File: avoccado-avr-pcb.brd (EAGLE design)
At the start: 17.8 x 33 mm, 32 parts, among them IC1 MCP1703CB, Q1 #MHz, Q2 MOSFET-NCHANNEL2N7002PW, U1 ATMEGA168#, U2 MCP73831, X1 Micro USB

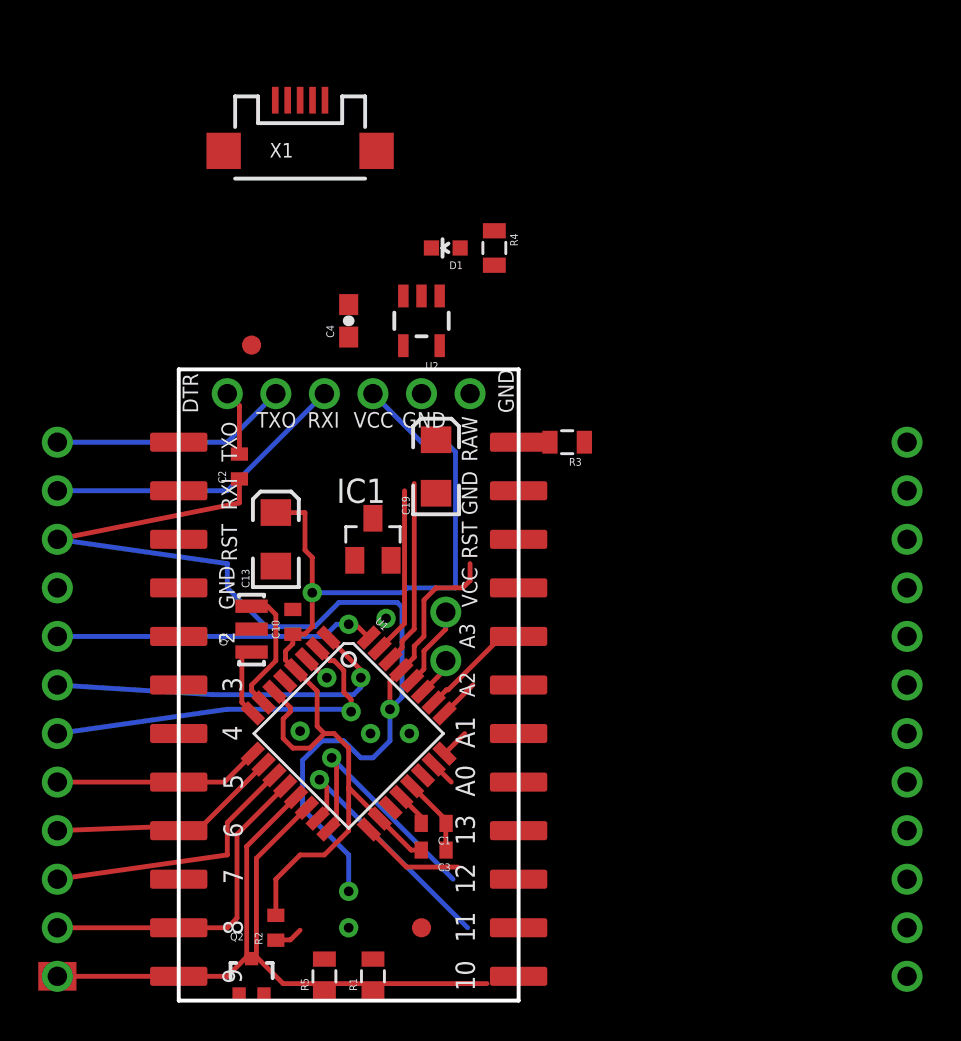
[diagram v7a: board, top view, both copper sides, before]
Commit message: squeezed the headers together to make the PCB even thinner
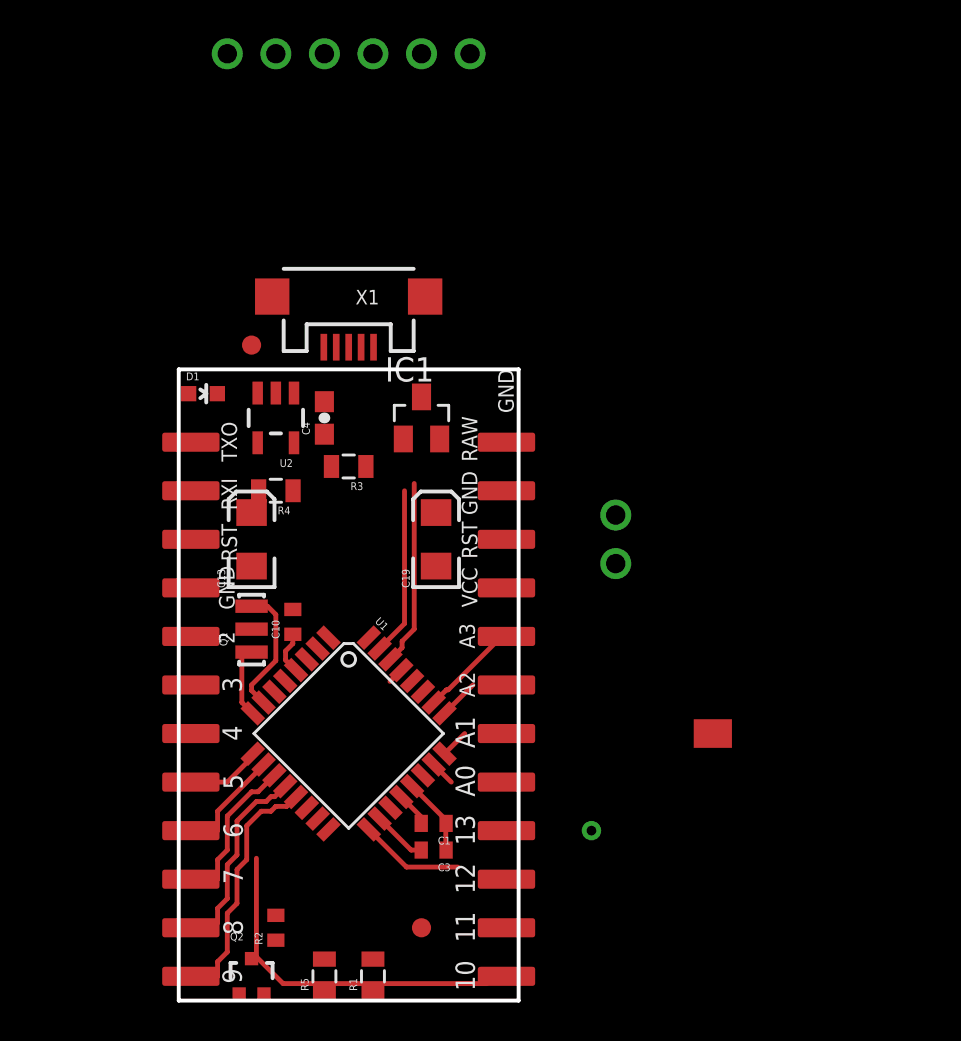
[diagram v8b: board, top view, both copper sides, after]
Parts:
- removed C2: 0.1uF, SparkFun:C0402
- removed JP6, JP7: (no value), SparkFun:1X12
- moved JP4 36.6 mm to (36.8, 25.4)
- moved JP1 17.8 mm to (11.4, 61.0)
- moved R4 17.1 mm to (14.0, 38.1), turned to 180 degrees
- moved D1 14.8 mm to (10.2, 43.2), turned to 270 degrees
- moved R3 11.5 mm to (17.8, 39.4)
- moved JP2 10.2 mm to (31.8, 34.3)
- moved U2 9.16 mm to (14.0, 41.9)
- moved X1 8.03 mm to (17.8, 48.3), turned to 180 degrees
- moved IC1 6.84 mm to (21.6, 41.9)
- moved C4 5.24 mm to (16.5, 41.9)
- moved C19 3.81 mm to (22.4, 35.6)
- moved C13 1.27 mm to (12.7, 35.6)
- moved JP3 0.64 mm to (26.0, 36.8)
- moved JP5 0.64 mm to (26.0, 26.7)
- moved JP8 0.64 mm to (26.0, 16.5)
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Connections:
- net A0: no longer JP6.8
- net A1: no longer JP6.7
- net A2: no longer JP6.6
- net A3: no longer JP6.5
- net D10: no longer JP6.12
- net D2: no longer JP7.8
- net D3: no longer JP7.7
- net D4: no longer JP7.6
- net D5-VIBR: no longer JP7.5
- net D6: no longer JP7.4
- net D7: no longer JP7.3
- net D8: no longer JP7.2
- net D9: no longer JP7.1
- net DTR: no longer C2.2
- net GND: no longer JP6.2, JP7.9
- net MISO: no longer JP6.10
- net MOSI: no longer JP6.11
- net RAW: no longer JP6.1
- net RESET: no longer C2.1, JP6.3, JP7.10
- net RXI: no longer JP7.11
- net SCK: no longer JP6.9
- net TXO: no longer JP7.12
- net VCC: no longer JP6.4
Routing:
- net RESET: track 64.3 -> 0.86 mm, vias 2 -> 0
- net VCC: track 59.0 -> 5.30 mm, vias 1 -> 0
- net D4: track 19.7 -> 0.00 mm, vias 1 -> 0
- net D3: track 19.4 -> 0.00 mm, vias 1 -> 0
- net D2: track 16.8 -> 0.00 mm, vias 1 -> 0
- net RXI: track 25.8 -> 9.71 mm
- net MOSI: track 13.3 -> 0.00 mm, vias 1 -> 0
- net MISO: track 13.0 -> 0.00 mm, vias 1 -> 0
- net TXO: track 21.3 -> 8.79 mm
- net D8: track 17.6 -> 10.5 mm
- net D5-VIBR: track 10.8 -> 3.94 mm
- net D9: track 19.8 -> 13.1 mm
- net D7: track 14.2 -> 8.26 mm
- net D6: track 12.1 -> 6.59 mm
- net A5: track 4.33 -> 0.00 mm
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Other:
- board text removed: "DTR"
